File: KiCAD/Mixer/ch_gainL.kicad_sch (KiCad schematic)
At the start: 8 parts, among them J4 Conn_01x02_Socket, J5 Conn_01x02_Socket, U1 NE5532

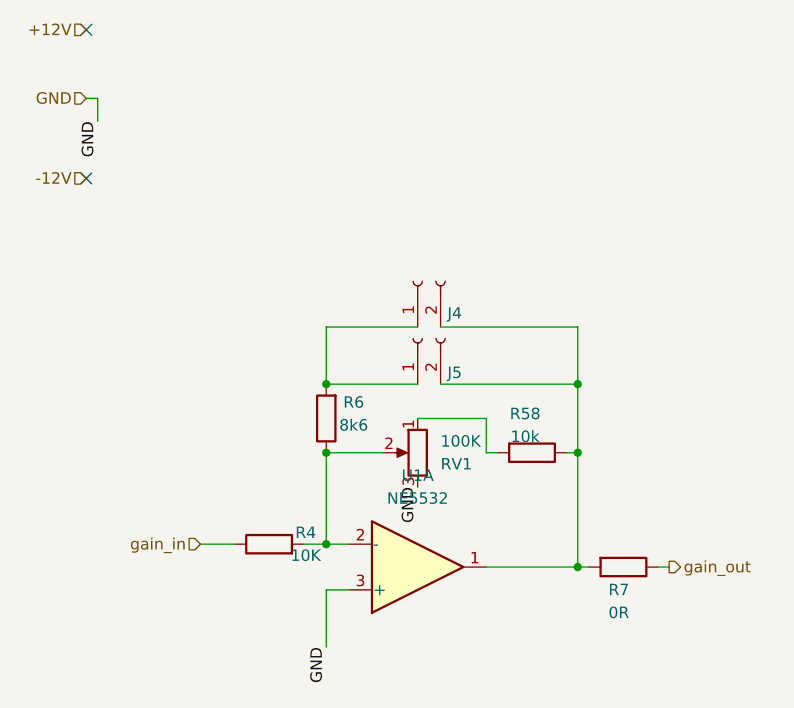
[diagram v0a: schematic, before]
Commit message: Rework of schematic, with error fixes and reworked pcb
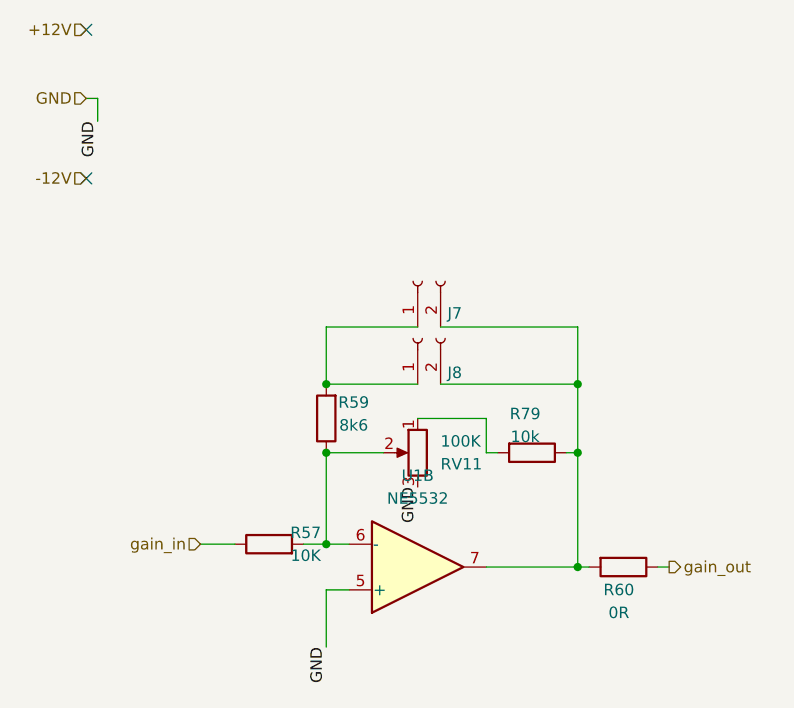
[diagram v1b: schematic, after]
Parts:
- removed U1: NE5532, Package_SO:SOIC-8_3.9x4.9mm_P1.27mm, symbol Amplifier_Operational:NE5532
- added U1: NE5532, Package_SO:SOIC-8_3.9x4.9mm_P1.27mm, symbol Amplifier_Operational:NE5532
- renumbered J4 to J7, J5 to J8, R4 to R57, R6 to R59, R7 to R60, R58 to R79, RV1 to RV11
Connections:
- net GND: now also U1.5 (+)
- net at J7.2 (Pin_2), J8.2 (Pin_2), R60.2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: now also U1.7
- net at R57.2, R59.1, RV11.2: now also U1.6 (-)
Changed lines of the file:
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@@
 		(in_pos_files yes)
 		(dnp no)
-		(property "Reference" "R7"
+		(property "Reference" "R60"
 			(at 111.252 86.36 90)
 			(show_name no)
@@
 		(instances
 			(project "Mixer"
-				(path "/322d427a-6aae-4762-92d6-d97688daf29b/8a2849b7-184d-4014-bb98-da9dec8b5f90/874eb9e3-c612-43fb-9dc5-24309708e7ee"
-					(reference "R7")
+				(path "/322d427a-6aae-4762-92d6-d97688daf29b/8a2849b7-184d-4014-bb98-da9dec8b5f90/afbffc69-b100-46db-9180-c5285a610f62"
+					(reference "R60")
 					(unit 1)
 				)
@@
 		(in_pos_files yes)
 		(dnp no)
-		(property "Reference" "J5"
+		(property "Reference" "J8"
 			(at 92.202 62.23 90)
 			(show_name no)
@@
 		(instances
 			(project "Mixer"
-				(path "/322d427a-6aae-4762-92d6-d97688daf29b/8a2849b7-184d-4014-bb98-da9dec8b5f90/874eb9e3-c612-43fb-9dc5-24309708e7ee"
-					(reference "J5")
+				(path "/322d427a-6aae-4762-92d6-d97688daf29b/8a2849b7-184d-4014-bb98-da9dec8b5f90/afbffc69-b100-46db-9180-c5285a610f62"
+					(reference "J8")
 					(unit 1)
 				)
@@
 		(in_pos_files yes)
 		(dnp no)
-		(property "Reference" "R6"
+		(property "Reference" "R59"
 			(at 81.788 65.532 0)
 			(show_name no)
@@
 		(instances
 			(project "Mixer"
-				(path "/322d427a-6aae-4762-92d6-d97688daf29b/8a2849b7-184d-4014-bb98-da9dec8b5f90/874eb9e3-c612-43fb-9dc5-24309708e7ee"
-					(reference "R6")
+				(path "/322d427a-6aae-4762-92d6-d97688daf29b/8a2849b7-184d-4014-bb98-da9dec8b5f90/afbffc69-b100-46db-9180-c5285a610f62"
+					(reference "R59")
 					(unit 1)
 				)
@@
 		(in_pos_files yes)
 		(dnp no)
-		(property "Reference" "J4"
+		(property "Reference" "J7"
 			(at 92.202 55.626 90)
 			(show_name no)
@@
 		(instances
 			(project "Mixer"
-				(path "/322d427a-6aae-4762-92d6-d97688daf29b/8a2849b7-184d-4014-bb98-da9dec8b5f90/874eb9e3-c612-43fb-9dc5-24309708e7ee"
-					(reference "J4")
+				(path "/322d427a-6aae-4762-92d6-d97688daf29b/8a2849b7-184d-4014-bb98-da9dec8b5f90/afbffc69-b100-46db-9180-c5285a610f62"
+					(reference "J7")
 					(unit 1)
 				)
@@
 		(in_pos_files yes)
 		(dnp no)
-		(property "Reference" "R58"
+		(property "Reference" "R79"
 			(at 100.838 66.802 90)
 			(show_name no)
@@
 		(instances
 			(project "Mixer"
-				(path "/322d427a-6aae-4762-92d6-d97688daf29b/8a2849b7-184d-4014-bb98-da9dec8b5f90/874eb9e3-c612-43fb-9dc5-24309708e7ee"
-					(reference "R58")
+				(path "/322d427a-6aae-4762-92d6-d97688daf29b/8a2849b7-184d-4014-bb98-da9dec8b5f90/afbffc69-b100-46db-9180-c5285a610f62"
+					(reference "R79")
 					(unit 1)
 				)
@@
 		(at 88.9 83.82 0)
 		(mirror x)
-		(unit 1)
+		(unit 2)
 		(body_style 1)
 		(exclude_from_sim no)
@@
 		(instances
 			(project "Mixer"
-				(path "/322d427a-6aae-4762-92d6-d97688daf29b/8a2849b7-184d-4014-bb98-da9dec8b5f90/874eb9e3-c612-43fb-9dc5-24309708e7ee"
+				(path "/322d427a-6aae-4762-92d6-d97688daf29b/8a2849b7-184d-4014-bb98-da9dec8b5f90/afbffc69-b100-46db-9180-c5285a610f62"
 					(reference "U1")
-					(unit 1)
+					(unit 2)
 				)
 			)
@@
 		(in_pos_files yes)
 		(dnp no)
-		(property "Reference" "R4"
+		(property "Reference" "R57"
 			(at 76.454 80.01 90)
 			(show_name no)
@@
 		(instances
 			(project "Mixer"
-				(path "/322d427a-6aae-4762-92d6-d97688daf29b/8a2849b7-184d-4014-bb98-da9dec8b5f90/874eb9e3-c612-43fb-9dc5-24309708e7ee"
-					(reference "R4")
+				(path "/322d427a-6aae-4762-92d6-d97688daf29b/8a2849b7-184d-4014-bb98-da9dec8b5f90/afbffc69-b100-46db-9180-c5285a610f62"
+					(reference "R57")
 					(unit 1)
 				)
@@
 		(in_pos_files yes)
 		(dnp no)
-		(property "Reference" "RV1"
+		(property "Reference" "RV11"
 			(at 91.44 72.39 0)
 			(show_name no)
@@
 		(instances
 			(project "Mixer"
-				(path "/322d427a-6aae-4762-92d6-d97688daf29b/8a2849b7-184d-4014-bb98-da9dec8b5f90/874eb9e3-c612-43fb-9dc5-24309708e7ee"
-					(reference "RV1")
+				(path "/322d427a-6aae-4762-92d6-d97688daf29b/8a2849b7-184d-4014-bb98-da9dec8b5f90/afbffc69-b100-46db-9180-c5285a610f62"
+					(reference "RV11")
 					(unit 1)
 				)

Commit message: Final PCB Version that got ordered from JLCPCB
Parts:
- removed R79: 10k, Resistor_SMD:R_0805_2012Metric_Pad1.20x1.40mm_HandSolder, symbol Device:R
- removed RV11: 100K, Potentiometer_THT:Potentiometer_Alps_RK09K_Single_Vertical, symbol Device:R_Potentiometer
- added R58: 8k6, Resistor_SMD:R_0805_2012Metric_Pad1.20x1.40mm_HandSolder, symbol Device:R
- added RV9: 100K, Potentiometer_THT:Potentiometer_Alps_RK09K_Single_Vertical, symbol Device:R_Potentiometer
- R59: value 8k6 -> 10k
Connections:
- net GND: now also RV9.3
- net at J7.2 (Pin_2), J8.2 (Pin_2), R60.2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: now also R59.1
- net at J7.1 (Pin_1), J8.1 (Pin_1): now also R58.2; no longer R59.2
- net at R57.2, U1.6 (-): now also R58.1, RV9.2; no longer R59.1
- new net: R59.2, RV9.1
